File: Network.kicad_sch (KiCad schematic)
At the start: 30 parts, among them J5 RJ45_HR913550A, U4 X1000, U7 RTL8201F

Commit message: Update (Display)
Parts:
- R32, R33: footprint (none) -> Resistor_SMD:R_0402_1005Metric
- U4: footprint (none) -> TheBrutzlers_Lib:BGA256C80P16X16_1300X1300X130N
- renumbered C65 to C66, C66 to C67, C67 to C68, C68 to C69, C69 to C70, C70 to C71, C71 to C72, C72 to C73
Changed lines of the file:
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@@
     (property "Reference" "R32" (id 0) (at 67.31 77.47 90))
     (property "Value" "1K" (id 1) (at 67.31 80.01 90))
-    (property "Footprint" "" (id 2) (at 67.31 78.232 90)
+    (property "Footprint" "Resistor_SMD:R_0402_1005Metric" (id 2) (at 67.31 78.232 90)
       (effects (font (size 1.27 1.27)) hide)
     )
@@
   (symbol (lib_id "Device:C") (at 106.68 43.18 180) (unit 1)
     (in_bom yes) (on_board yes)
-    (property "Reference" "C69" (id 0) (at 111.76 41.91 0))
+    (property "Reference" "C70" (id 0) (at 111.76 41.91 0))
     (property "Value" "100n" (id 1) (at 111.76 44.45 0))
     (property "Footprint" "Capacitor_SMD:C_0402_1005Metric" (id 2) (at 105.7148 39.37 0)
@@
   (symbol (lib_id "Device:C") (at 163.83 59.69 270) (unit 1)
     (in_bom yes) (on_board yes)
-    (property "Reference" "C72" (id 0) (at 166.37 58.42 90))
+    (property "Reference" "C73" (id 0) (at 166.37 58.42 90))
     (property "Value" "100n" (id 1) (at 167.64 60.96 90))
     (property "Footprint" "Capacitor_SMD:C_0402_1005Metric" (id 2) (at 160.02 60.6552 0)
@@
   (symbol (lib_id "Device:C") (at 106.68 58.42 180) (unit 1)
     (in_bom yes) (on_board yes)
-    (property "Reference" "C70" (id 0) (at 111.76 57.15 0))
+    (property "Reference" "C71" (id 0) (at 111.76 57.15 0))
     (property "Value" "100n" (id 1) (at 111.76 59.69 0))
     (property "Footprint" "Capacitor_SMD:C_0402_1005Metric" (id 2) (at 105.7148 54.61 0)
@@
   (symbol (lib_id "Device:C") (at 100.33 43.18 180) (unit 1)
     (in_bom yes) (on_board yes)
-    (property "Reference" "C67" (id 0) (at 95.25 41.91 0))
+    (property "Reference" "C68" (id 0) (at 95.25 41.91 0))
     (property "Value" "1µ" (id 1) (at 95.25 44.45 0))
     (property "Footprint" "Capacitor_SMD:C_0402_1005Metric" (id 2) (at 99.3648 39.37 0)
@@
   (symbol (lib_id "Device:C") (at 100.33 58.42 180) (unit 1)
     (in_bom yes) (on_board yes)
-    (property "Reference" "C68" (id 0) (at 95.25 57.15 0))
+    (property "Reference" "C69" (id 0) (at 95.25 57.15 0))
     (property "Value" "1µ" (id 1) (at 95.25 59.69 0))
     (property "Footprint" "Capacitor_SMD:C_0402_1005Metric" (id 2) (at 99.3648 54.61 0)
@@
     (property "Reference" "R33" (id 0) (at 67.31 85.09 90))
     (property "Value" "1K" (id 1) (at 67.31 87.63 90))
-    (property "Footprint" "" (id 2) (at 67.31 85.852 90)
+    (property "Footprint" "Resistor_SMD:R_0402_1005Metric" (id 2) (at 67.31 85.852 90)
       (effects (font (size 1.27 1.27)) hide)
     )
@@
     (property "Reference" "U4" (id 0) (at 220.98 41.91 0))
     (property "Value" "X1000" (id 1) (at 220.98 44.45 0))
-    (property "Footprint" "" (id 2) (at 199.39 59.69 0)
+    (property "Footprint" "TheBrutzlers_Lib:BGA256C80P16X16_1300X1300X130N" (id 2) (at 199.39 59.69 0)
       (effects (font (size 1.27 1.27)) (justify left) hide)
     )
@@
   (symbol (lib_id "Device:C") (at 163.83 54.61 270) (unit 1)
     (in_bom yes) (on_board yes)
-    (property "Reference" "C71" (id 0) (at 166.37 53.34 90))
+    (property "Reference" "C72" (id 0) (at 166.37 53.34 90))
     (property "Value" "100n" (id 1) (at 167.64 55.88 90))
     (property "Footprint" "Capacitor_SMD:C_0402_1005Metric" (id 2) (at 160.02 55.5752 0)
@@
   (symbol (lib_id "Device:C") (at 69.85 72.39 90) (unit 1)
     (in_bom yes) (on_board yes)
-    (property "Reference" "C66" (id 0) (at 66.04 71.12 90))
+    (property "Reference" "C67" (id 0) (at 66.04 71.12 90))
     (property "Value" "100n" (id 1) (at 74.93 71.12 90))
     (property "Footprint" "Capacitor_SMD:C_0402_1005Metric" (id 2) (at 73.66 71.4248 0)
@@
   (symbol (lib_id "Device:C") (at 69.85 64.77 90) (unit 1)
     (in_bom yes) (on_board yes)
-    (property "Reference" "C65" (id 0) (at 66.04 63.5 90))
+    (property "Reference" "C66" (id 0) (at 66.04 63.5 90))
     (property "Value" "100n" (id 1) (at 74.93 63.5 90))
     (property "Footprint" "Capacitor_SMD:C_0402_1005Metric" (id 2) (at 73.66 63.8048 0)

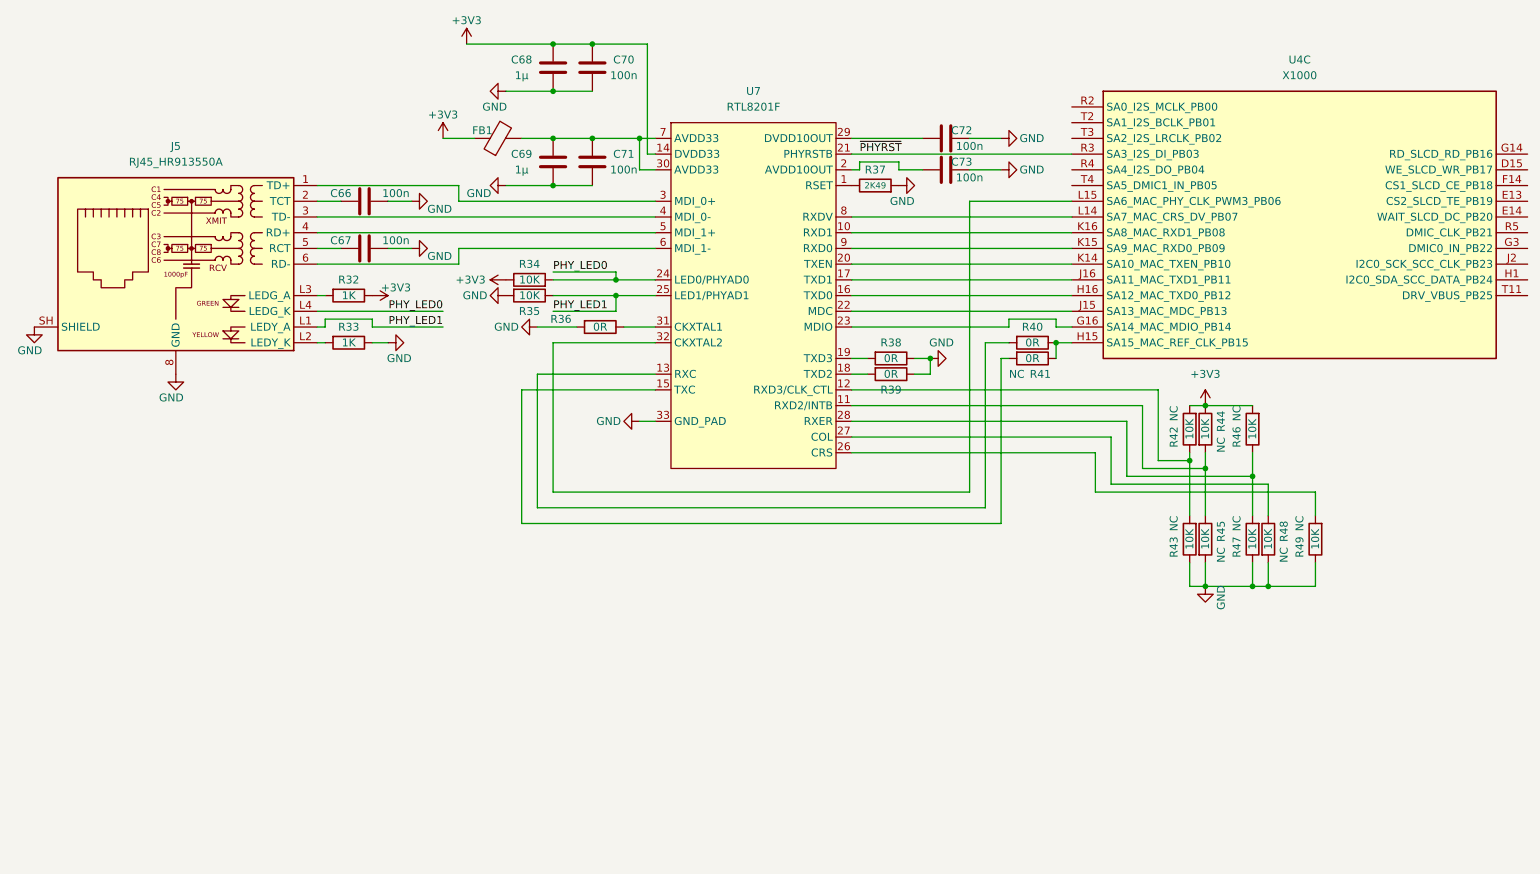
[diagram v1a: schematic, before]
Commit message: Add Audio
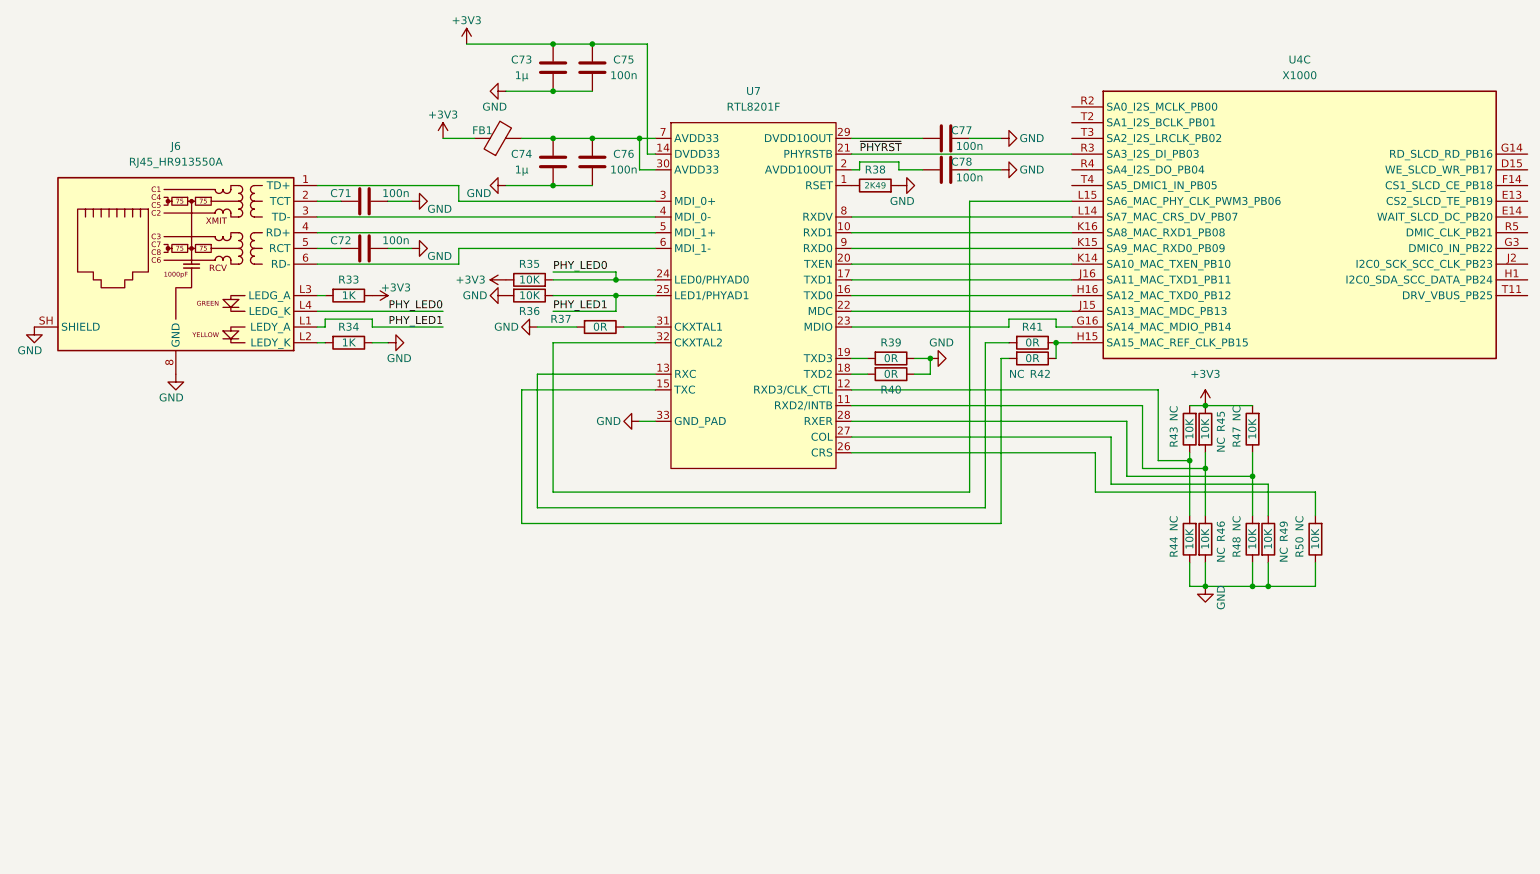
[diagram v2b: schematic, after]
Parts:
- J6: renamed from J5; LCSC (none) -> C163507
- renumbered C66 to C71, C67 to C72, C68 to C73, C69 to C74, C70 to C75, C71 to C76, C72 to C77, C73 to C78, R32 to R33, R33 to R34, R34 to R35, R35 to R36, R36 to R37, R37 to R38, R38 to R39, R39 to R40, R40 to R41, R41 to R42, R42 to R43, R43 to R44, R44 to R45, R45 to R46, R46 to R47, R47 to R48, R48 to R49, R49 to R50

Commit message: New i.mx6 Version
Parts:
- added U?: IMX6UL, TheBrutzlers_Lib:IMX6UL_BGA289, symbol TheBrutzlers_Lib:IMX6UL

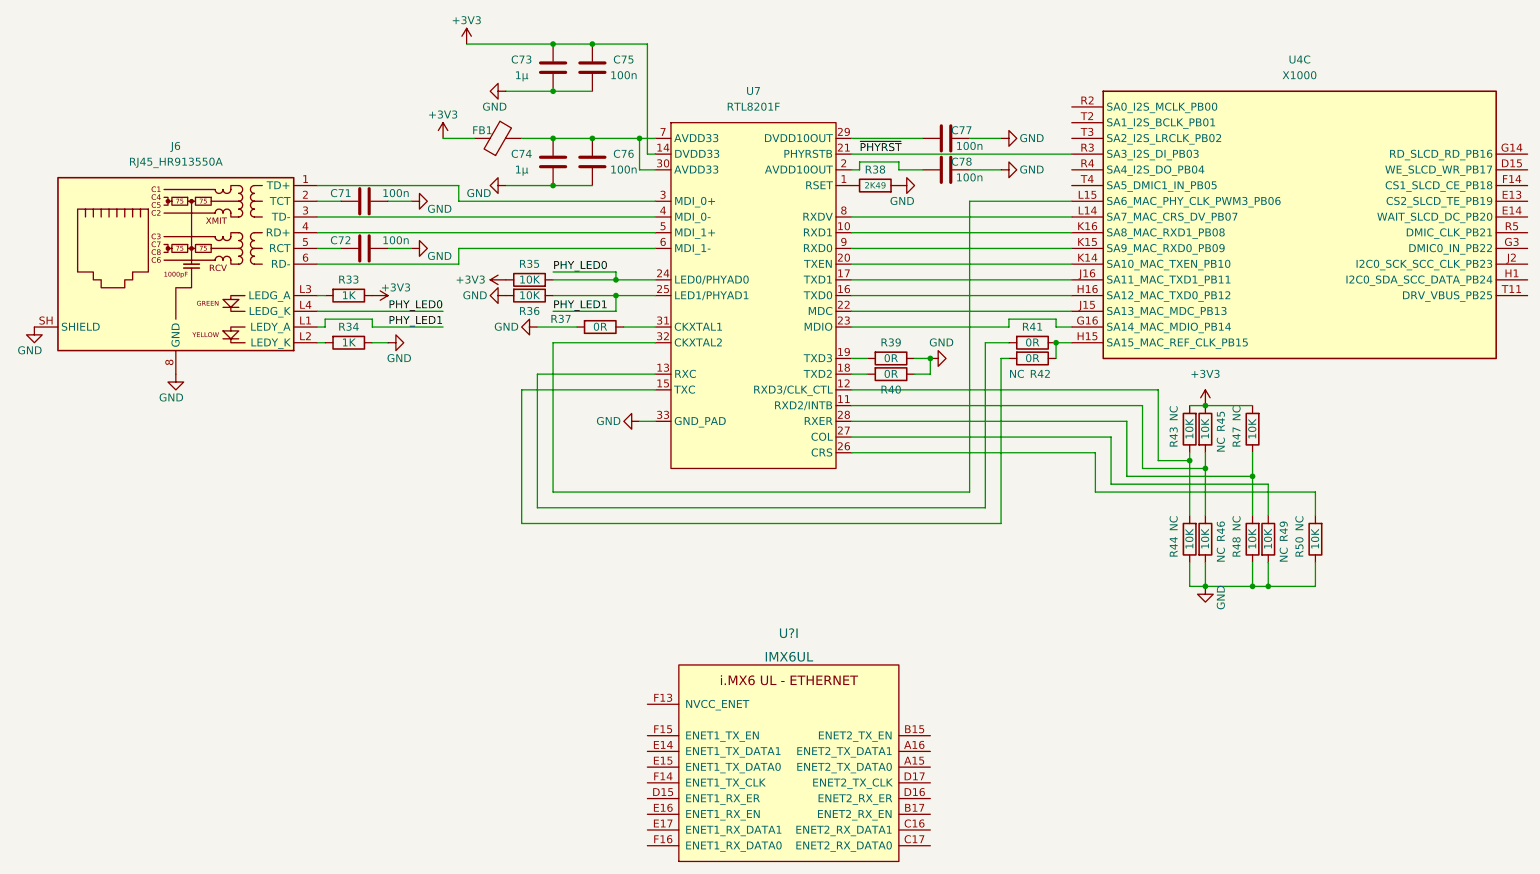
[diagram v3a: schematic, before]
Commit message: Display Update
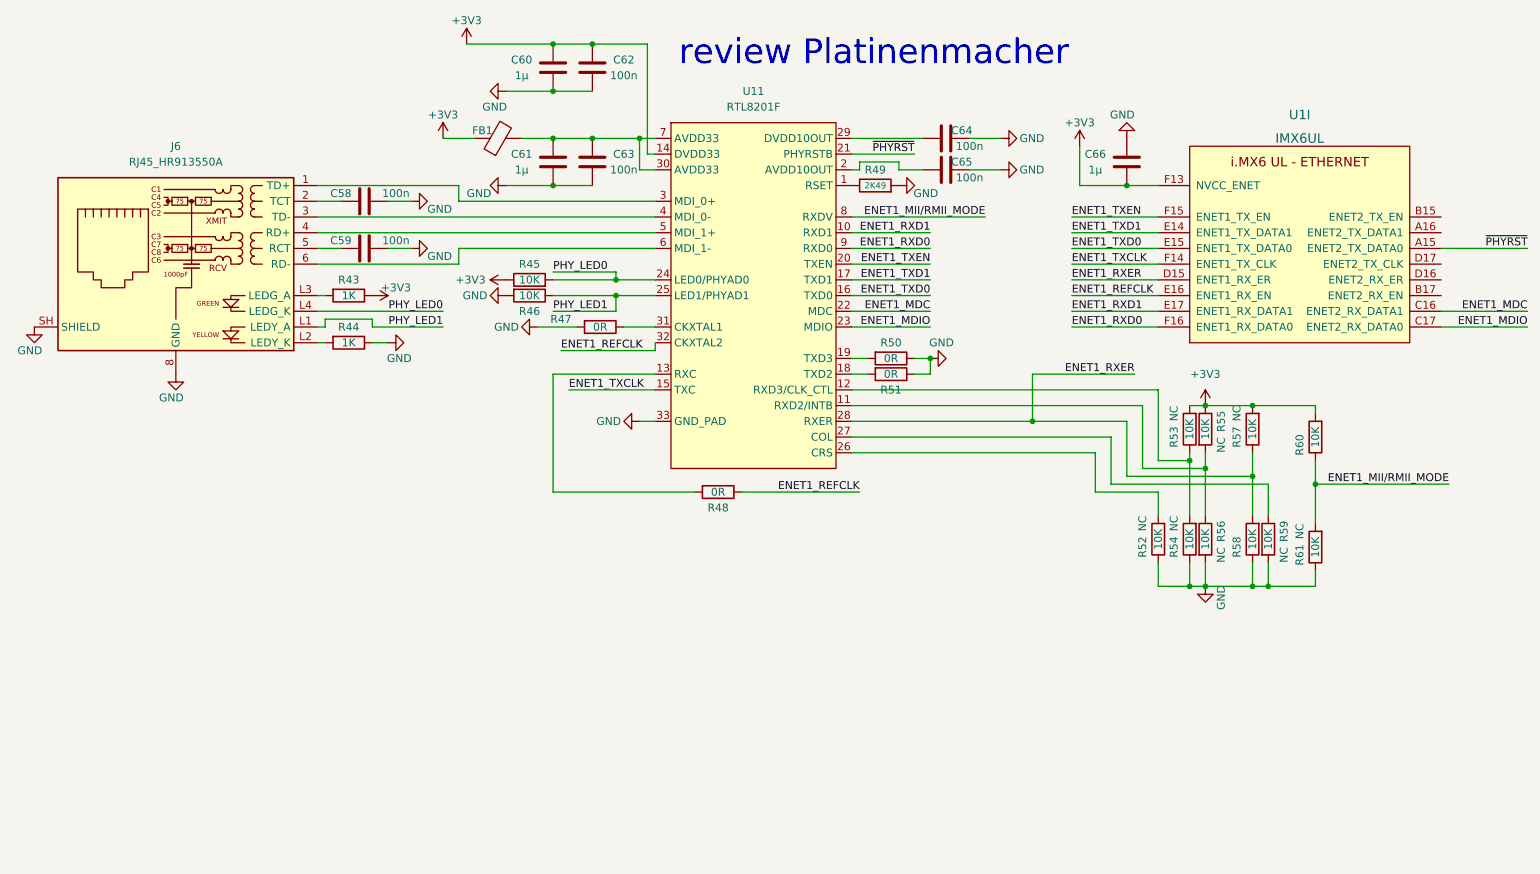
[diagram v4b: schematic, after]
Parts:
- removed R41, R42: 0R, symbol Device:R
- removed U4: X1000, TheBrutzlers_Lib:BGA256C80P16X16_1300X1300X130N, symbol TheBrutzlers_Lib:X1000
- added C66: 1µ, Capacitor_SMD:C_0402_1005Metric, symbol Device:C
- added R48: 0R, symbol Device:R
- added R60, R61: 10K, symbol Device:R
- R58: renamed from R48; populated NC -> (none)
- gave numbers to parts that had none: 1
- renumbered C71 to C58, C72 to C59, C73 to C60, C74 to C61, C75 to C62, C76 to C63, C77 to C64, C78 to C65, R33 to R43, R34 to R44, R35 to R45, R36 to R46, R37 to R47, R38 to R49, R39 to R50, R40 to R51, R50 to R52, R43 to R53, R44 to R54, R45 to R55, R46 to R56, R47 to R57, R49 to R59, U7 to U11
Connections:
- net +3V3: now also U1.F13 (NVCC_ENET), C66.1, R60.2
- net GND: now also C66.2, R61.1
- net ~{PHYRST}: now also U1.A15 (ENET2_TX_DATA0)
- net at U11.13 (RXC): now also R48.2
- net ENET1_TXCLK: now reaches U11.15 (TXC)
- net ENET1_TXCLK: now also U1.F14 (ENET1_TX_CLK)
- net ENET1_RXD1: now reaches U11.10 (RXD1)
- net ENET1_RXD1: now also U1.E17 (ENET1_RX_DATA1)
- net ENET1_TXD0: now reaches U11.16 (TXD0)
- net ENET1_TXD0: now also U1.E15 (ENET1_TX_DATA0)
- net ENET1_TXD1: now reaches U11.17 (TXD1)
- net ENET1_TXD1: now also U1.E14 (ENET1_TX_DATA1)
- net ENET1_TXEN: now reaches U11.20 (TXEN)
- net ENET1_TXEN: now also U1.F15 (ENET1_TX_EN)
- net ENET1_MDC: now reaches U11.22 (MDC)
- net ENET1_MDC: now also U1.C16 (ENET2_RX_DATA1)
- net ENET1_MDIO: now reaches U11.23 (MDIO)
- net ENET1_MDIO: now also U1.C17 (ENET2_RX_DATA0)
- net ENET1_RXER: now reaches R57.1, R58.2, U11.28 (RXER)
- net ENET1_RXER: now also U1.D15 (ENET1_RX_ER)
- net ENET1_REFCLK: now reaches U11.32 (CKXTAL2)
- net ENET1_REFCLK: now also U1.E16 (ENET1_RX_EN), R48.1
- net ENET1_MII/RMII_MODE: now reaches U11.8 (RXDV)
- net ENET1_MII/RMII_MODE: now also R60.1, R61.2
- net ENET1_RXD0: now reaches U11.9 (RXD0)
- net ENET1_RXD0: now also U1.F16 (ENET1_RX_DATA0)
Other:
- note added: "review Platinenmacher"
- moved on the sheet: R52, U1I
